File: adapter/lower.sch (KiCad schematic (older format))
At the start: 13 parts, among them J1 MALE, J2 FEMALE, J3 STANDOFF, J4 STANDOFF, J5 DTR

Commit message: Finish schematic
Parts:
- removed FB?: Ferrite_Bead_Small, symbol Device:Ferrite_Bead_Small
- removed J3, J4: STANDOFF, symbol Connector_Generic:Conn_01x01
- removed J?: USB_B, symbol Connector:USB_B
- added D1: Red, LED_SMD:LED_0805_2012Metric_Pad1.15x1.40mm_HandSolder, symbol Device:LED_Small
- added D2: Green, LED_SMD:LED_0805_2012Metric_Pad1.15x1.40mm_HandSolder, symbol Device:LED_Small
- added J3: USB_C_Receptacle_USB2.0, symbol Connector:USB_C_Receptacle_USB2.0
- added R1, R2: 1k, Resistor_SMD:R_0805_2012Metric_Pad1.20x1.40mm_HandSolder, symbol Device:R_Small_US
- C1, C2, C3, C4: renamed from C?; footprint (none) -> Capacitor_SMD:C_0805_2012Metric_Pad1.15x1.40mm_HandSolder
- F1: renamed from F?; footprint (none) -> Fuse:Fuse_0805_2012Metric_Pad1.15x1.40mm_HandSolder
- J1: footprint (none) -> Connector_PinHeader_2.54mm:PinHeader_2x02_P2.54mm_Horizontal; symbol Connector_Generic:Conn_02x02_Counter_Clockwise -> Connector_Generic:Conn_02x02_Top_Bottom
- J2: footprint (none) -> Connector_PinSocket_2.54mm:PinSocket_2x02_P2.54mm_Vertical; symbol Connector_Generic:Conn_02x02_Counter_Clockwise -> Connector_Generic:Conn_02x02_Odd_Even
- J5: footprint (none) -> Connector_PinHeader_2.54mm:PinHeader_1x01_P2.54mm_Vertical
- gave numbers to parts that had none: 1
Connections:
- net labels added: D+, D-, VBUS
- wire segments 68 -> 74
- no-connect marks 11 -> 15
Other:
- moved on the sheet: C1, F1

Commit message: Assign USB receptacle
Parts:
- J3: footprint (none) -> node:SOFNG_MC-311D
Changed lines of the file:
@@
 F 0 "J3" H 1657 5367 50  0000 C CNN
 F 1 "USB_C_Receptacle_USB2.0" H 1657 5276 50  0000 C CNN
-F 2 "" H 1700 4500 50  0001 C CNN
+F 2 "node:SOFNG_MC-311D" H 1700 4500 50  0001 C CNN
 F 3 "https://www.usb.org/sites/default/files/documents/usb_type-c.zip" H 1700 4500 50  0001 C CNN
 	1    1550 4500

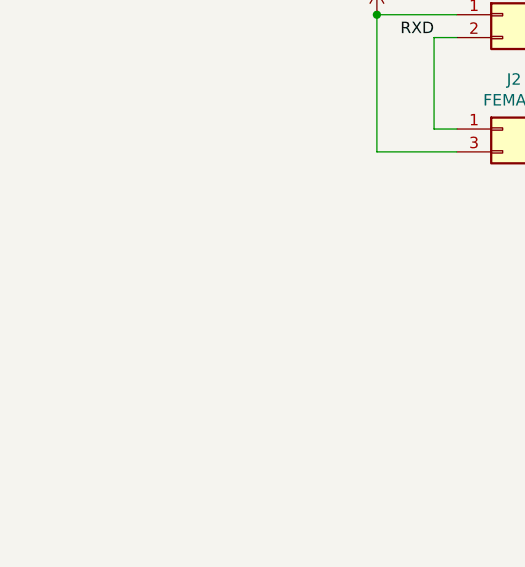
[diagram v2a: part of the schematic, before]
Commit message: Add power flags
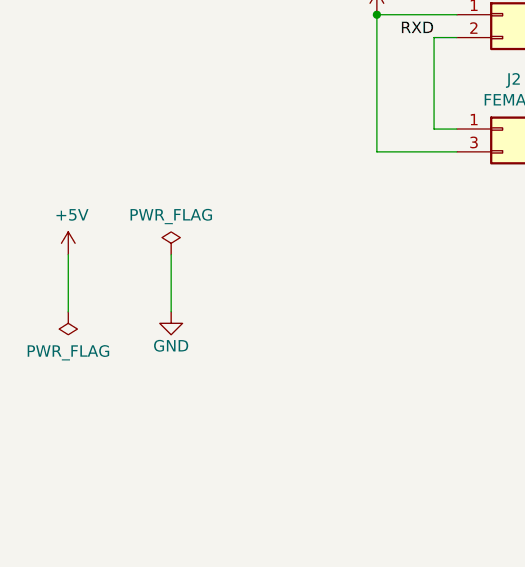
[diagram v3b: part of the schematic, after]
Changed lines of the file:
@@
 NoConn ~ 2150 5000
 NoConn ~ 2150 5100
+$Comp
+L power:+5V #PWR?
+U 1 1 5FB6B75B
+P 1200 2200
+F 0 "#PWR?" H 1200 2050 50  0001 C CNN
+F 1 "+5V" H 1215 2373 50  0000 C CNN
+F 2 "" H 1200 2200 50  0001 C CNN
+F 3 "" H 1200 2200 50  0001 C CNN
+	1    1200 2200
+	1    0    0    -1
+$EndComp
+$Comp
+L power:GND #PWR?
+U 1 1 5FB6B9B3
+P 1650 2450
+F 0 "#PWR?" H 1650 2200 50  0001 C CNN
+F 1 "GND" H 1650 2300 50  0000 C CNN
+F 2 "" H 1650 2450 50  0001 C CNN
+F 3 "" H 1650 2450 50  0001 C CNN
+	1    1650 2450
+	1    0    0    -1
+$EndComp
+$Comp
+L power:PWR_FLAG #FLG?
+U 1 1 5FB6BD0D
+P 1650 2200
+F 0 "#FLG?" H 1650 2275 50  0001 C CNN
+F 1 "PWR_FLAG" H 1650 2373 50  0000 C CNN
+F 2 "" H 1650 2200 50  0001 C CNN
+F 3 "~" H 1650 2200 50  0001 C CNN
+	1    1650 2200
+	1    0    0    -1
+$EndComp
+$Comp
+L power:PWR_FLAG #FLG?
+U 1 1 5FB6BDD6
+P 1200 2450
+F 0 "#FLG?" H 1200 2525 50  0001 C CNN
+F 1 "PWR_FLAG" H 1200 2623 50  0000 C CNN
+F 2 "" H 1200 2450 50  0001 C CNN
+F 3 "~" H 1200 2450 50  0001 C CNN
+	1    1200 2450
+	-1   0    0    1
+$EndComp
+Wire Wire Line
+	1200 2200 1200 2450
+Wire Wire Line
+	1650 2200 1650 2450
 $EndSCHEMATC

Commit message: Change female headers to horizontal
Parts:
- J2: footprint Connector_PinSocket_2.54mm:PinSocket_2x02_P2.54mm_Vertical -> Connector_PinSocket_2.54mm:PinSocket_2x02_P2.54mm_Horizontal
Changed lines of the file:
@@
 F 0 "J2" H 3150 1867 50  0000 C CNN
 F 1 "FEMALE" H 3150 1776 50  0000 C CNN
-F 2 "Connector_PinSocket_2.54mm:PinSocket_2x02_P2.54mm_Vertical" H 3100 1650 50  0001 C CNN
+F 2 "Connector_PinSocket_2.54mm:PinSocket_2x02_P2.54mm_Horizontal" H 3100 1650 50  0001 C CNN
 F 3 "~" H 3100 1650 50  0001 C CNN
 	1    3100 1650
@@
 NoConn ~ 2150 5100
 $Comp
-L power:+5V #PWR?
+L power:+5V #PWR0113
 U 1 1 5FB6B75B
 P 1200 2200
-F 0 "#PWR?" H 1200 2050 50  0001 C CNN
+F 0 "#PWR0113" H 1200 2050 50  0001 C CNN
 F 1 "+5V" H 1215 2373 50  0000 C CNN
 F 2 "" H 1200 2200 50  0001 C CNN
@@
 $EndComp
 $Comp
-L power:GND #PWR?
+L power:GND #PWR0114
 U 1 1 5FB6B9B3
 P 1650 2450
-F 0 "#PWR?" H 1650 2200 50  0001 C CNN
+F 0 "#PWR0114" H 1650 2200 50  0001 C CNN
 F 1 "GND" H 1650 2300 50  0000 C CNN
 F 2 "" H 1650 2450 50  0001 C CNN
@@
 $EndComp
 $Comp
-L power:PWR_FLAG #FLG?
+L power:PWR_FLAG #FLG0101
 U 1 1 5FB6BD0D
 P 1650 2200
-F 0 "#FLG?" H 1650 2275 50  0001 C CNN
+F 0 "#FLG0101" H 1650 2275 50  0001 C CNN
 F 1 "PWR_FLAG" H 1650 2373 50  0000 C CNN
 F 2 "" H 1650 2200 50  0001 C CNN
@@
 $EndComp
 $Comp
-L power:PWR_FLAG #FLG?
+L power:PWR_FLAG #FLG0102
 U 1 1 5FB6BDD6
 P 1200 2450
-F 0 "#FLG?" H 1200 2525 50  0001 C CNN
+F 0 "#FLG0102" H 1200 2525 50  0001 C CNN
 F 1 "PWR_FLAG" H 1200 2623 50  0000 C CNN
 F 2 "" H 1200 2450 50  0001 C CNN

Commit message: Use 1206 pad for fuse
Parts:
- F1: footprint Fuse:Fuse_0805_2012Metric_Pad1.15x1.40mm_HandSolder -> Fuse:Fuse_1206_3216Metric_Pad1.42x1.75mm_HandSolder
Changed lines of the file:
@@
 F 0 "F1" V 7045 2200 50  0000 C CNN
 F 1 "Polyfuse_Small" V 7136 2200 50  0000 C CNN
-F 2 "Fuse:Fuse_0805_2012Metric_Pad1.15x1.40mm_HandSolder" H 7300 2000 50  0001 L CNN
+F 2 "Fuse:Fuse_1206_3216Metric_Pad1.42x1.75mm_HandSolder" H 7300 2000 50  0001 L CNN
 F 3 "~" H 7250 2200 50  0001 C CNN
 	1    7250 2200

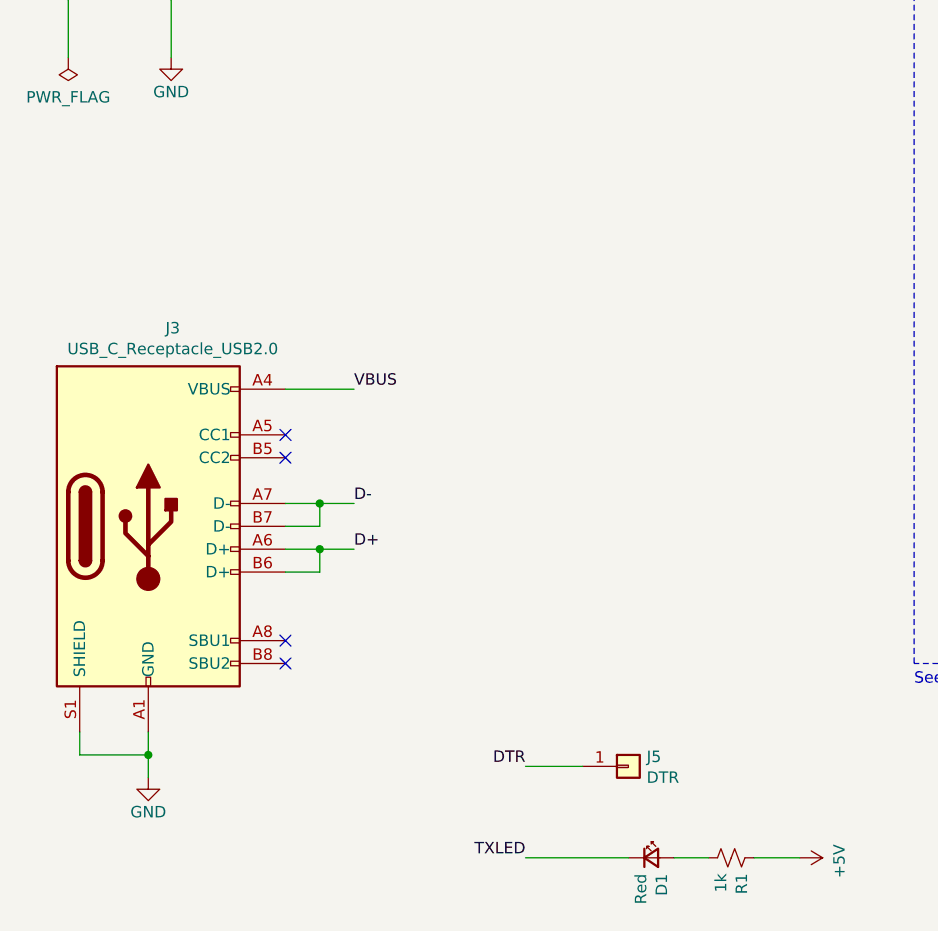
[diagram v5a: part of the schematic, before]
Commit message: Add holes for standoffs
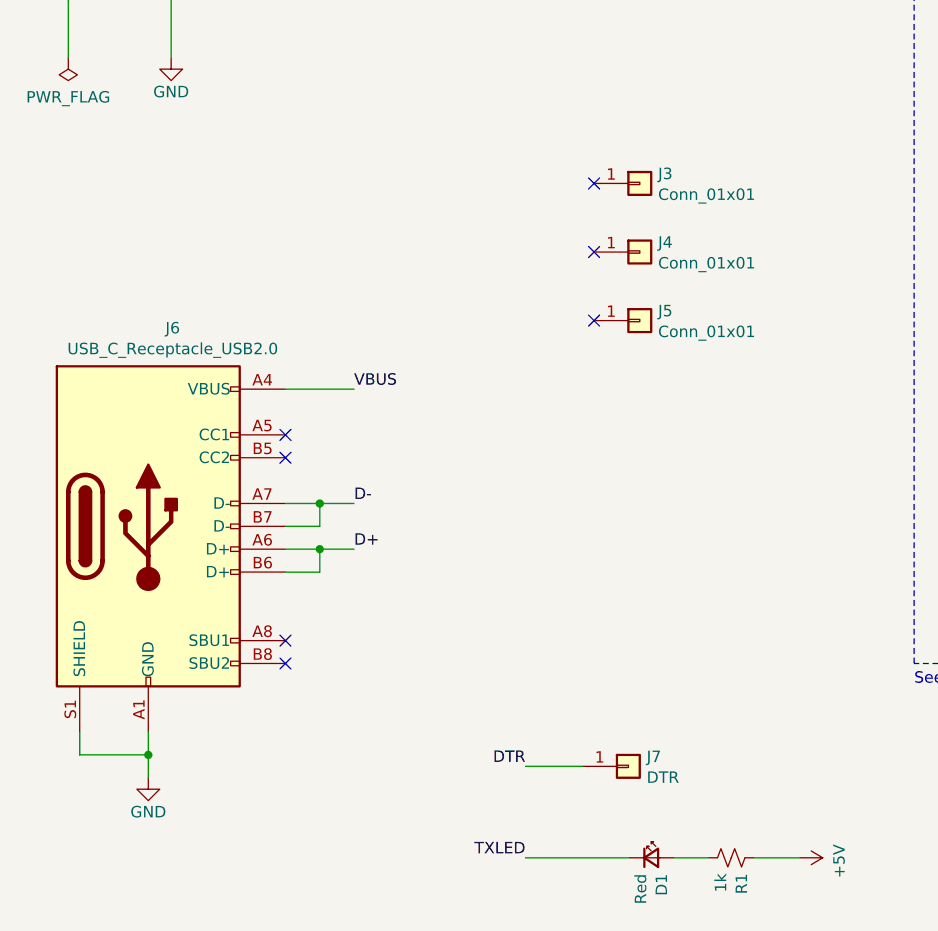
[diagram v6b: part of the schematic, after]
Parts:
- added J3, J4, J5: Conn_01x01, MountingHole:MountingHole_2.2mm_M2_Pad_Via, symbol Connector_Generic:Conn_01x01
- renumbered J3 to J6, J5 to J7
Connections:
- no-connect marks 15 -> 18
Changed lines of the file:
@@
 $EndDescr
 $Comp
-L Connector_Generic:Conn_01x01 J5
+L Connector_Generic:Conn_01x01 J7
 U 1 1 5FA6E68E
 P 3650 5550
-F 0 "J5" H 3730 5592 50  0000 L CNN
+F 0 "J7" H 3730 5592 50  0000 L CNN
 F 1 "DTR" H 3730 5501 50  0000 L CNN
 F 2 "Connector_PinHeader_2.54mm:PinHeader_1x01_P2.54mm_Vertical" H 3650 5550 50  0001 C CNN
@@
 Connection ~ 1550 5500
 $Comp
-L Connector:USB_C_Receptacle_USB2.0 J3
+L Connector:USB_C_Receptacle_USB2.0 J6
 U 1 1 5FBA90B8
 P 1550 4500
-F 0 "J3" H 1657 5367 50  0000 C CNN
+F 0 "J6" H 1657 5367 50  0000 C CNN
 F 1 "USB_C_Receptacle_USB2.0" H 1657 5276 50  0000 C CNN
 F 2 "node:SOFNG_MC-311D" H 1700 4500 50  0001 C CNN
@@
 Wire Wire Line
 	1650 2200 1650 2450
+$Comp
+L Connector_Generic:Conn_01x01 J3
+U 1 1 5FB8A10A
+P 3700 3000
+F 0 "J3" H 3780 3042 50  0000 L CNN
+F 1 "Conn_01x01" H 3780 2951 50  0000 L CNN
+F 2 "MountingHole:MountingHole_2.2mm_M2_Pad_Via" H 3700 3000 50  0001 C CNN
+F 3 "~" H 3700 3000 50  0001 C CNN
+	1    3700 3000
+	1    0    0    -1
+$EndComp
+NoConn ~ 3500 3000
+$Comp
+L Connector_Generic:Conn_01x01 J4
+U 1 1 5FB8C43D
+P 3700 3300
+F 0 "J4" H 3780 3342 50  0000 L CNN
+F 1 "Conn_01x01" H 3780 3251 50  0000 L CNN
+F 2 "MountingHole:MountingHole_2.2mm_M2_Pad_Via" H 3700 3300 50  0001 C CNN
+F 3 "~" H 3700 3300 50  0001 C CNN
+	1    3700 3300
+	1    0    0    -1
+$EndComp
+$Comp
+L Connector_Generic:Conn_01x01 J5
+U 1 1 5FB8C4F1
+P 3700 3600
+F 0 "J5" H 3780 3642 50  0000 L CNN
+F 1 "Conn_01x01" H 3780 3551 50  0000 L CNN
+F 2 "MountingHole:MountingHole_2.2mm_M2_Pad_Via" H 3700 3600 50  0001 C CNN
+F 3 "~" H 3700 3600 50  0001 C CNN
+	1    3700 3600
+	1    0    0    -1
+$EndComp
+NoConn ~ 3500 3300
+NoConn ~ 3500 3600
 $EndSCHEMATC

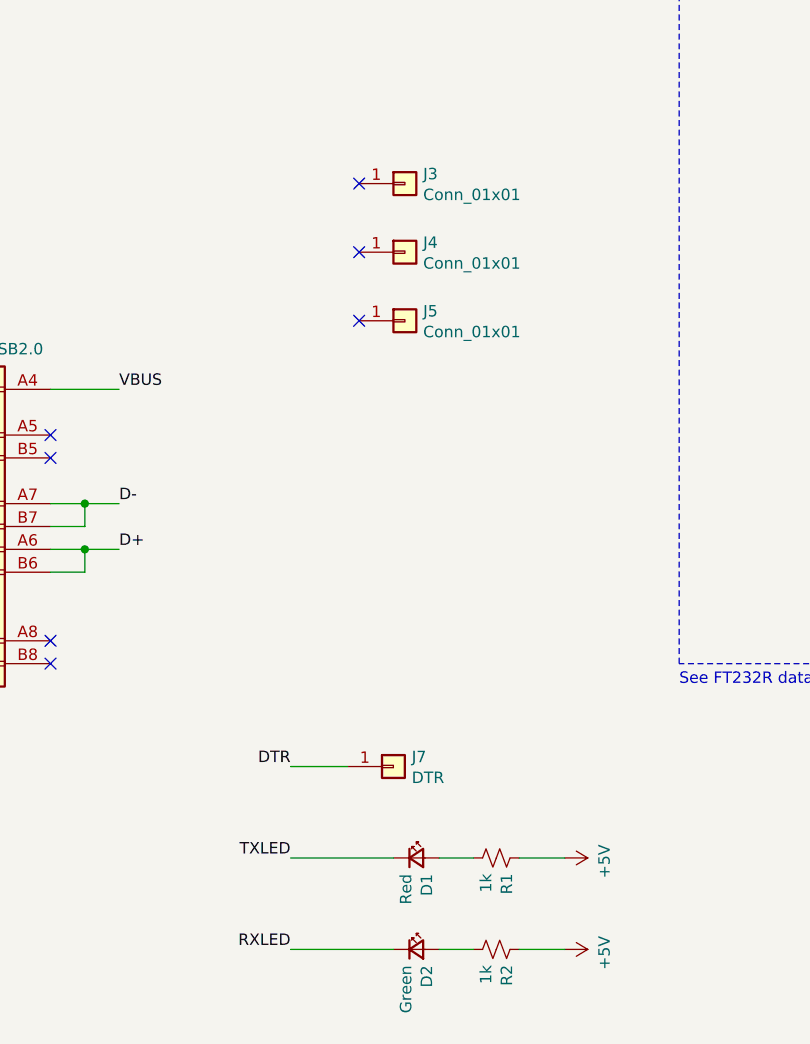
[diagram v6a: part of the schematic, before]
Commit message: Move LEDs to upper board
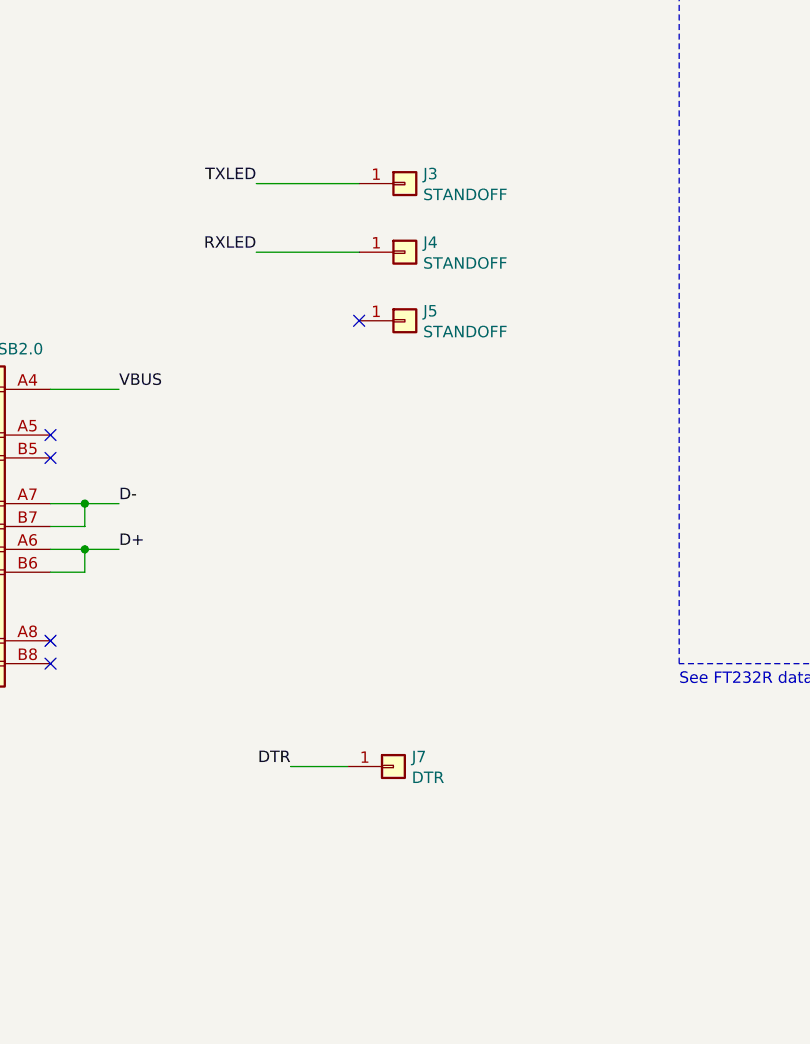
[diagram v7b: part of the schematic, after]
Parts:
- removed D1: Red, LED_SMD:LED_0805_2012Metric_Pad1.15x1.40mm_HandSolder, symbol Device:LED_Small
- removed D2: Green, LED_SMD:LED_0805_2012Metric_Pad1.15x1.40mm_HandSolder, symbol Device:LED_Small
- removed R1, R2: 1k, Resistor_SMD:R_0805_2012Metric_Pad1.20x1.40mm_HandSolder, symbol Device:R_Small_US
- J3, J4, J5: value Conn_01x01 -> STANDOFF
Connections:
- net RXLED: now also J4.1 (Pin_1)
- net TXLED: now also J3.1 (Pin_1)
- no-connect marks 18 -> 16
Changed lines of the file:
@@
 Text Label 8800 4100 0    50   ~ 0
 RXLED
-Text Label 3200 5950 2    50   ~ 0
+Text Label 3050 3000 2    50   ~ 0
 TXLED
-Text Label 3200 6350 2    50   ~ 0
+Text Label 3050 3300 2    50   ~ 0
 RXLED
 NoConn ~ 8650 4200
@@
 Wire Wire Line
 	2800 1650 2900 1650
-$Comp
-L power:+5V #PWR0108
-U 1 1 5FB52707
-P 4400 5950
-AR Path="/5FA6C89B/5FB52707" Ref="#PWR0108"  Part="1"
-AR Path="/5FA6C6C8/5FB52707" Ref="#PWR?"  Part="1"
-F 0 "#PWR0108" H 4400 5800 50  0001 C CNN
-F 1 "+5V" H 4415 6123 50  0000 C CNN
-F 2 "" H 4400 5950 50  0001 C CNN
-F 3 "" H 4400 5950 50  0001 C CNN
-	1    4400 5950
-	0    1    1    0
-$EndComp
-$Comp
-L Device:R_Small_US R?
-U 1 1 5FB5270D
-P 4100 5950
-AR Path="/5FA6C6C8/5FB5270D" Ref="R?"  Part="1"
-AR Path="/5FA6C89B/5FB5270D" Ref="R1"  Part="1"
-F 0 "R1" H 4168 5996 50  0000 L CNN
-F 1 "1k" H 4168 5905 50  0000 L CNN
-F 2 "Resistor_SMD:R_0805_2012Metric_Pad1.20x1.40mm_HandSolder" H 4100 5950 50  0001 C CNN
-F 3 "~" H 4100 5950 50  0001 C CNN
-	1    4100 5950
-	0    1    1    0
-$EndComp
-$Comp
-L Device:LED_Small D?
-U 1 1 5FB52713
-P 3750 5950
-AR Path="/5FA6C6C8/5FB52713" Ref="D?"  Part="1"
-AR Path="/5FA6C89B/5FB52713" Ref="D1"  Part="1"
-F 0 "D1" V 3796 5880 50  0000 R CNN
-F 1 "Red" V 3705 5880 50  0000 R CNN
-F 2 "LED_SMD:LED_0805_2012Metric_Pad1.15x1.40mm_HandSolder" V 3750 5950 50  0001 C CNN
-F 3 "~" V 3750 5950 50  0001 C CNN
-	1    3750 5950
-	1    0    0    -1
-$EndComp
-Wire Wire Line
-	4400 5950 4200 5950
-Wire Wire Line
-	4000 5950 3850 5950
-$Comp
-L Device:LED_Small D?
-U 1 1 5FB5271C
-P 3750 6350
-AR Path="/5FA6C6C8/5FB5271C" Ref="D?"  Part="1"
-AR Path="/5FA6C89B/5FB5271C" Ref="D2"  Part="1"
-F 0 "D2" V 3796 6280 50  0000 R CNN
-F 1 "Green" V 3705 6280 50  0000 R CNN
-F 2 "LED_SMD:LED_0805_2012Metric_Pad1.15x1.40mm_HandSolder" V 3750 6350 50  0001 C CNN
-F 3 "~" V 3750 6350 50  0001 C CNN
-	1    3750 6350
-	1    0    0    -1
-$EndComp
-$Comp
-L Device:R_Small_US R?
-U 1 1 5FB52722
-P 4100 6350
-AR Path="/5FA6C6C8/5FB52722" Ref="R?"  Part="1"
-AR Path="/5FA6C89B/5FB52722" Ref="R2"  Part="1"
-F 0 "R2" H 4168 6396 50  0000 L CNN
-F 1 "1k" H 4168 6305 50  0000 L CNN
-F 2 "Resistor_SMD:R_0805_2012Metric_Pad1.20x1.40mm_HandSolder" H 4100 6350 50  0001 C CNN
-F 3 "~" H 4100 6350 50  0001 C CNN
-	1    4100 6350
-	0    1    1    0
-$EndComp
-$Comp
-L power:+5V #PWR0109
-U 1 1 5FB52728
-P 4400 6350
-AR Path="/5FA6C89B/5FB52728" Ref="#PWR0109"  Part="1"
-AR Path="/5FA6C6C8/5FB52728" Ref="#PWR?"  Part="1"
-F 0 "#PWR0109" H 4400 6200 50  0001 C CNN
-F 1 "+5V" H 4415 6523 50  0000 C CNN
-F 2 "" H 4400 6350 50  0001 C CNN
-F 3 "" H 4400 6350 50  0001 C CNN
-	1    4400 6350
-	0    1    1    0
-$EndComp
-Wire Wire Line
-	4200 6350 4400 6350
-Wire Wire Line
-	4000 6350 3850 6350
-Wire Wire Line
-	3200 5950 3650 5950
-Wire Wire Line
-	3200 6350 3650 6350
+Wire Wire Line
+	3050 3000 3500 3000
+Wire Wire Line
+	3050 3300 3500 3300
 Wire Wire Line
 	2150 3900 2450 3900
@@
 	1650 2200 1650 2450
 $Comp
+L Connector_Generic:Conn_01x01 J5
+U 1 1 5FB8C4F1
+P 3700 3600
+F 0 "J5" H 3780 3642 50  0000 L CNN
+F 1 "STANDOFF" H 3780 3551 50  0000 L CNN
+F 2 "MountingHole:MountingHole_2.2mm_M2_Pad_Via" H 3700 3600 50  0001 C CNN
+F 3 "~" H 3700 3600 50  0001 C CNN
+	1    3700 3600
+	1    0    0    -1
+$EndComp
+NoConn ~ 3500 3600
+$Comp
+L Connector_Generic:Conn_01x01 J4
+U 1 1 5FB8C43D
+P 3700 3300
+F 0 "J4" H 3780 3342 50  0000 L CNN
+F 1 "STANDOFF" H 3780 3251 50  0000 L CNN
+F 2 "MountingHole:MountingHole_2.2mm_M2_Pad_Via" H 3700 3300 50  0001 C CNN
+F 3 "~" H 3700 3300 50  0001 C CNN
+	1    3700 3300
+	1    0    0    -1
+$EndComp
+$Comp
 L Connector_Generic:Conn_01x01 J3
 U 1 1 5FB8A10A
 P 3700 3000
 F 0 "J3" H 3780 3042 50  0000 L CNN
-F 1 "Conn_01x01" H 3780 2951 50  0000 L CNN
+F 1 "STANDOFF" H 3780 2951 50  0000 L CNN
 F 2 "MountingHole:MountingHole_2.2mm_M2_Pad_Via" H 3700 3000 50  0001 C CNN
 F 3 "~" H 3700 3000 50  0001 C CNN
@@
 	1    0    0    -1
 $EndComp
-NoConn ~ 3500 3000
-$Comp
-L Connector_Generic:Conn_01x01 J4
-U 1 1 5FB8C43D
-P 3700 3300
-F 0 "J4" H 3780 3342 50  0000 L CNN
-F 1 "Conn_01x01" H 3780 3251 50  0000 L CNN
-F 2 "MountingHole:MountingHole_2.2mm_M2_Pad_Via" H 3700 3300 50  0001 C CNN
-F 3 "~" H 3700 3300 50  0001 C CNN
-	1    3700 3300
-	1    0    0    -1
-$EndComp
-$Comp
-L Connector_Generic:Conn_01x01 J5
-U 1 1 5FB8C4F1
-P 3700 3600
-F 0 "J5" H 3780 3642 50  0000 L CNN
-F 1 "Conn_01x01" H 3780 3551 50  0000 L CNN
-F 2 "MountingHole:MountingHole_2.2mm_M2_Pad_Via" H 3700 3600 50  0001 C CNN
-F 3 "~" H 3700 3600 50  0001 C CNN
-	1    3700 3600
-	1    0    0    -1
-$EndComp
-NoConn ~ 3500 3300
-NoConn ~ 3500 3600
 $EndSCHEMATC
